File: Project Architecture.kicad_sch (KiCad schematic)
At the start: 0 parts

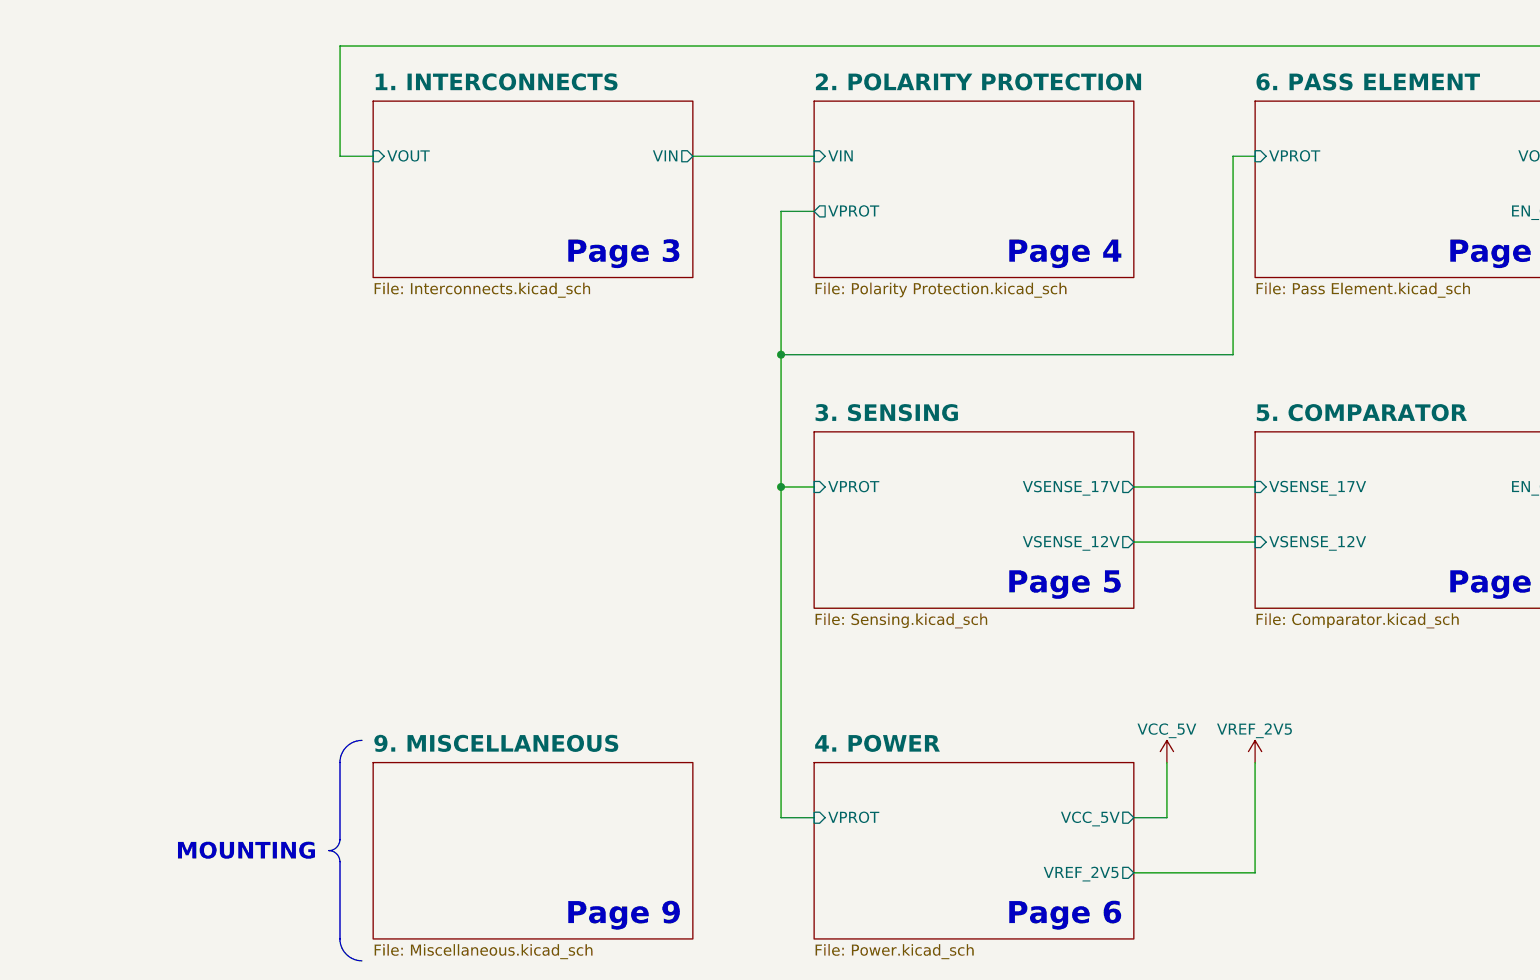
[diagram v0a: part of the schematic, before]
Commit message: feat!: added OC protection, redesigned board from near scratch, size increase
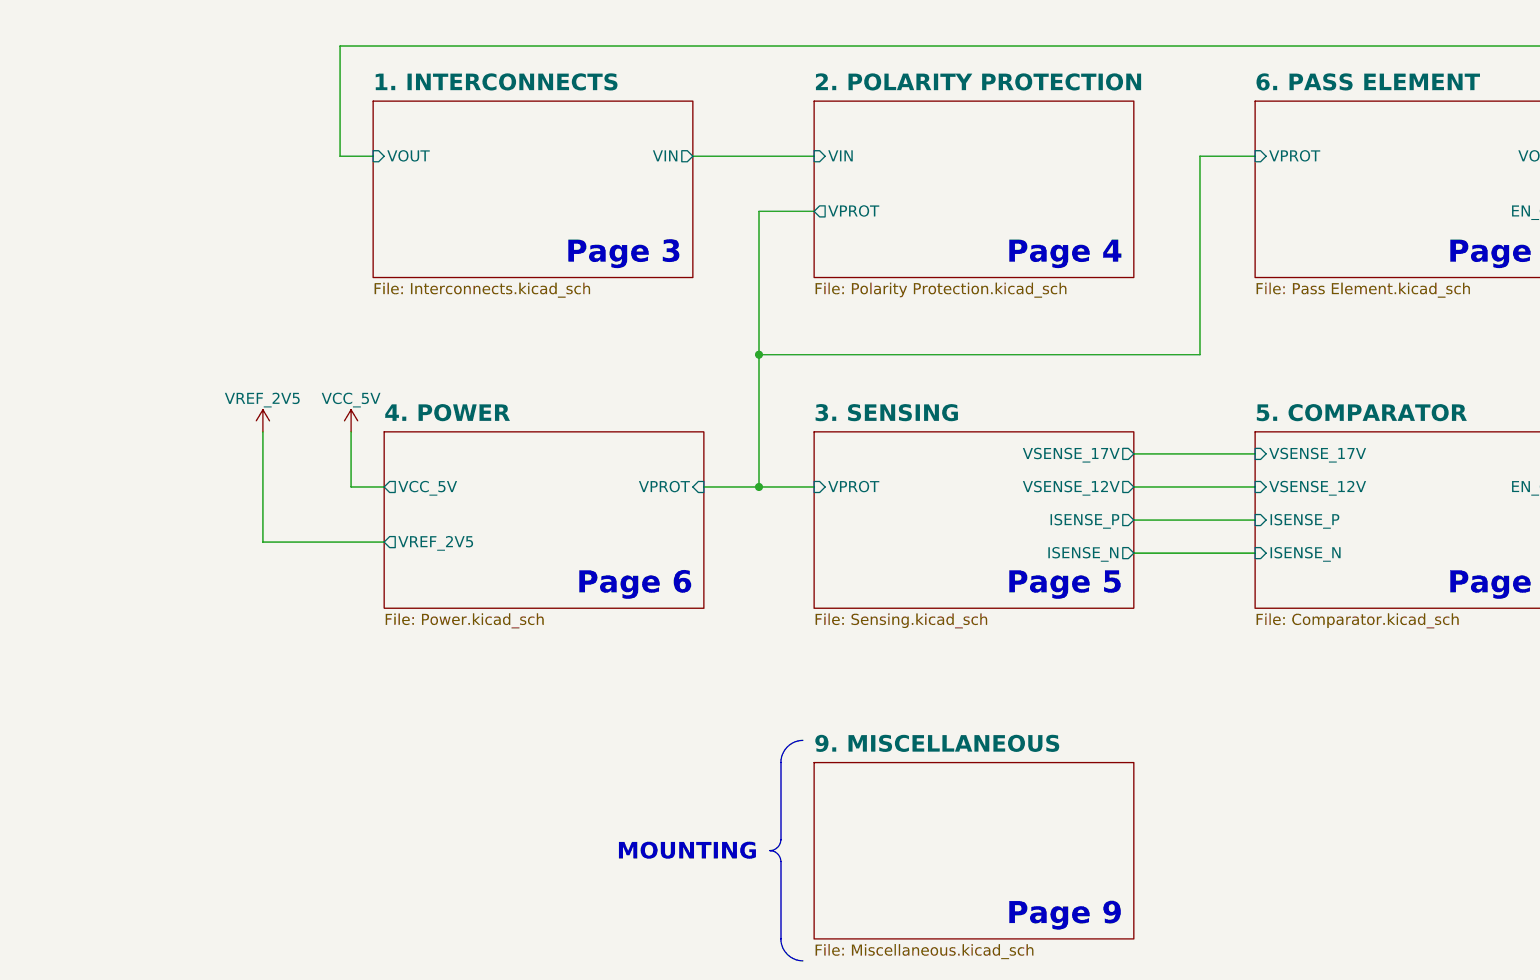
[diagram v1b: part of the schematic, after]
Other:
- sheet 3. SENSING ports: added ISENSE_N, ISENSE_P; removed none
- sheet 5. COMPARATOR ports: added ISENSE_N, ISENSE_P; removed none
